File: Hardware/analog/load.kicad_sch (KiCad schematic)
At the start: 21 parts, among them J201 Würth 74651194R, J202 Würth 74651194R, Q201 IXTH80N075L2, U201 ADA4522-2, U202 LM431SC

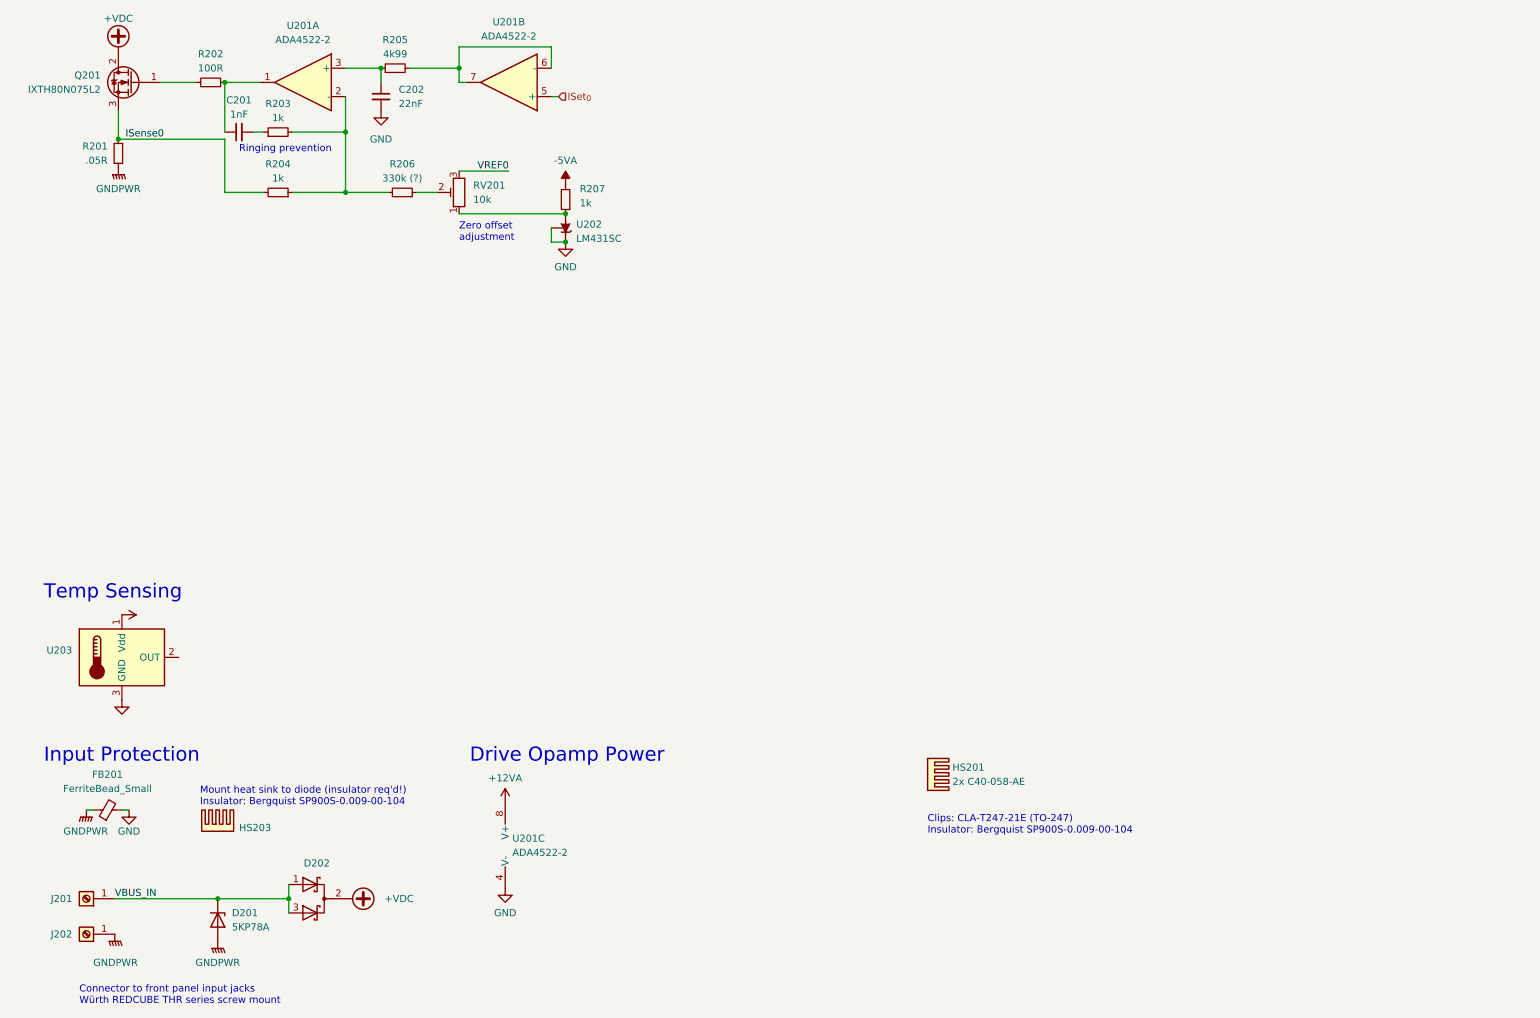
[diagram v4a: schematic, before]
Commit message: Work on layout analog board
- Moved the heatsink to be horizontal near the bottom of the analog
  board, to give more open space for the analog circuitry away from the
  hot MOSFETs

- Minor tweak to bonus display (cutout for front panel jacks)
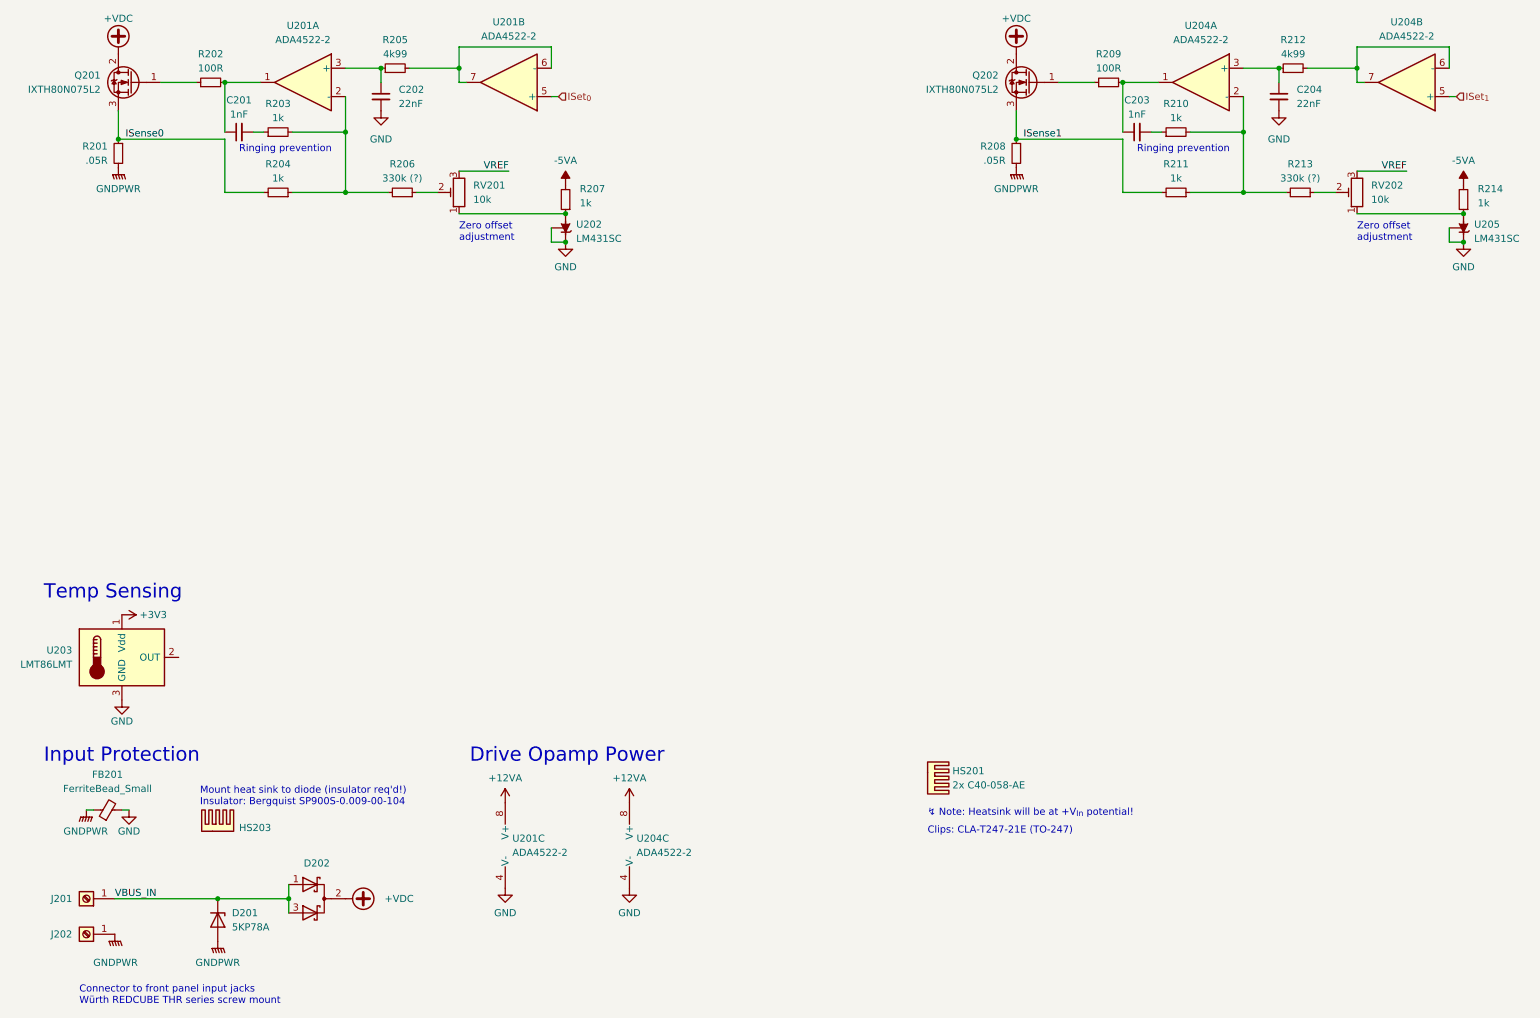
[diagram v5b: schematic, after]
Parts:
- added C203: 1nF, Capacitor_SMD:C_0805_2012Metric_Pad1.18x1.45mm_HandSolder, symbol Device:C_Small
- added C204: 22nF, Capacitor_SMD:C_0805_2012Metric_Pad1.18x1.45mm_HandSolder, symbol Device:C_Small
- added Q202: IXTH80N075L2, Package_TO_SOT_THT:TO-247-3_Vertical, symbol programmable-load:IXTH80N075L2
- added R208: .05R, programmable-load:TO-247-2_Vertical, symbol Device:R_Small
- added R209: 100R, Resistor_SMD:R_0805_2012Metric_Pad1.20x1.40mm_HandSolder, symbol Device:R_Small
- added R210, R211, R214: 1k, Resistor_SMD:R_0805_2012Metric_Pad1.20x1.40mm_HandSolder, symbol Device:R_Small
- added R212: 4k99, Resistor_SMD:R_0805_2012Metric_Pad1.20x1.40mm_HandSolder, symbol Device:R_Small
- added R213: 330k (?), Resistor_SMD:R_0805_2012Metric_Pad1.20x1.40mm_HandSolder, symbol Device:R_Small
- added RV202: 10k, programmable-load:Potentiometer_Nidec_Copal_CT94EY, symbol Device:R_Potentiometer_Trim
- added U204: ADA4522-2, Package_SO:SOIC-8_3.9x4.9mm_P1.27mm, symbol programmable-load:ADA4522-2R
- added U205: LM431SC, Package_TO_SOT_SMD:SOT-23, symbol Reference_Voltage:TL431DBZ
- U203: value (none) -> LMT86LMT
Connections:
- net +12VA: now also U204.8 (V+)
- net +VDC: now also Q202.2 (D)
- net -5VA: now also R214.2
- net GND: now also C204.2, U204.4 (V-), U205.1 (K), U205.2 (REF)
- net GNDPWR: now also R208.2
- net VREF0 renamed VREF
- net VREF: now also RV202.3
- new net: C203.1, R209.2, U204.1
- new net: R210.2, R211.1, R213.2, U204.2 (-)
- new net: C204.1, R212.1, U204.3 (+)
- new net: Q202.1 (G), R209.1
- new net: C203.2, R210.1
- new net: R213.1, RV202.2
- new net: R214.1, RV202.1, U205.3 (A)
- new net: R212.2, U204.6 (-), U204.7
- new net ISense1: Q202.3 (S), R208.1, R211.2
- new net ISet_{1}: U204.5 (+)
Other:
- note added: "Clips: CLA-T247-21E (TO-247)"
- note added: "↯ Note: Heatsink will be at +V_{In} potential!"
- note removed: "Clips: CLA-T247-21E (TO-247) Insulator: Bergquist SP900S-0.009-00-104"
- moved on the sheet: HS201

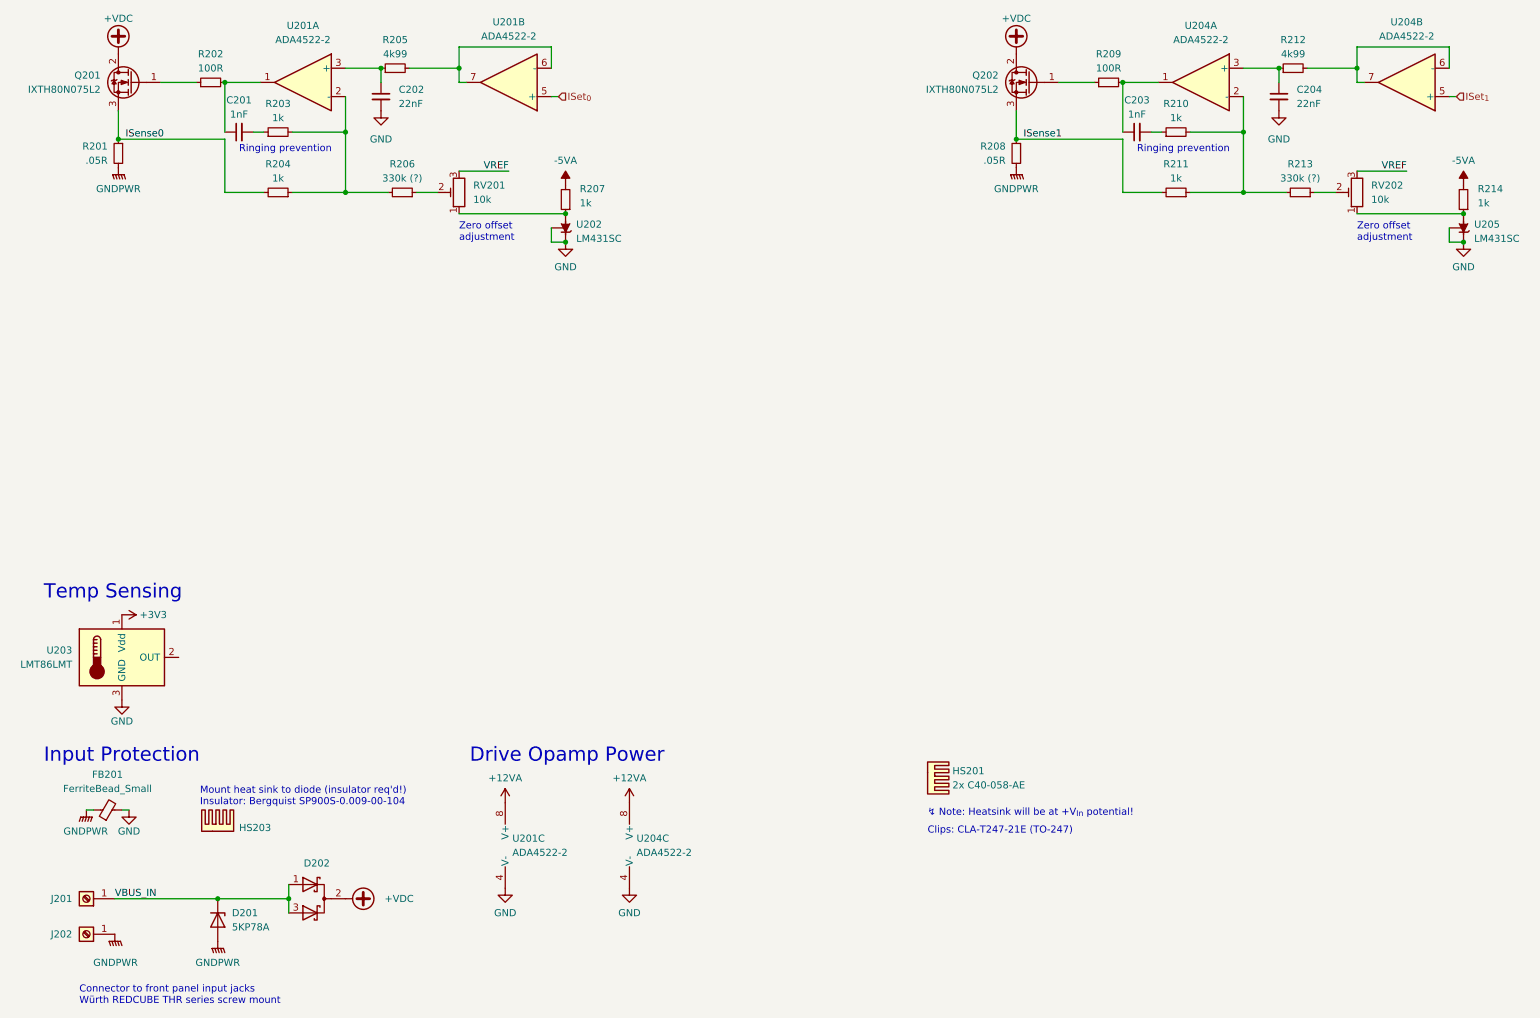
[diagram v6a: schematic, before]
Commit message: Initial pass at analog board
- Everything currently in the schematic is routed, and stuff is
  reasonably sanely laid out

- Some compromises: namely, the zero offset doesn't use the DAC
  reference for its positive, but generates a separate 2.5V via the
  shunt diodes; this is then shared between both op-amps. That avoids
  the DAC/ADC reference getting noisified

  Also, we don't have an ADC for measuring the temperature sensors yet,
  and in fact, those aren't routed out (or existent really) yet either

- TODO: add test points for drive voltages and current sense voltages
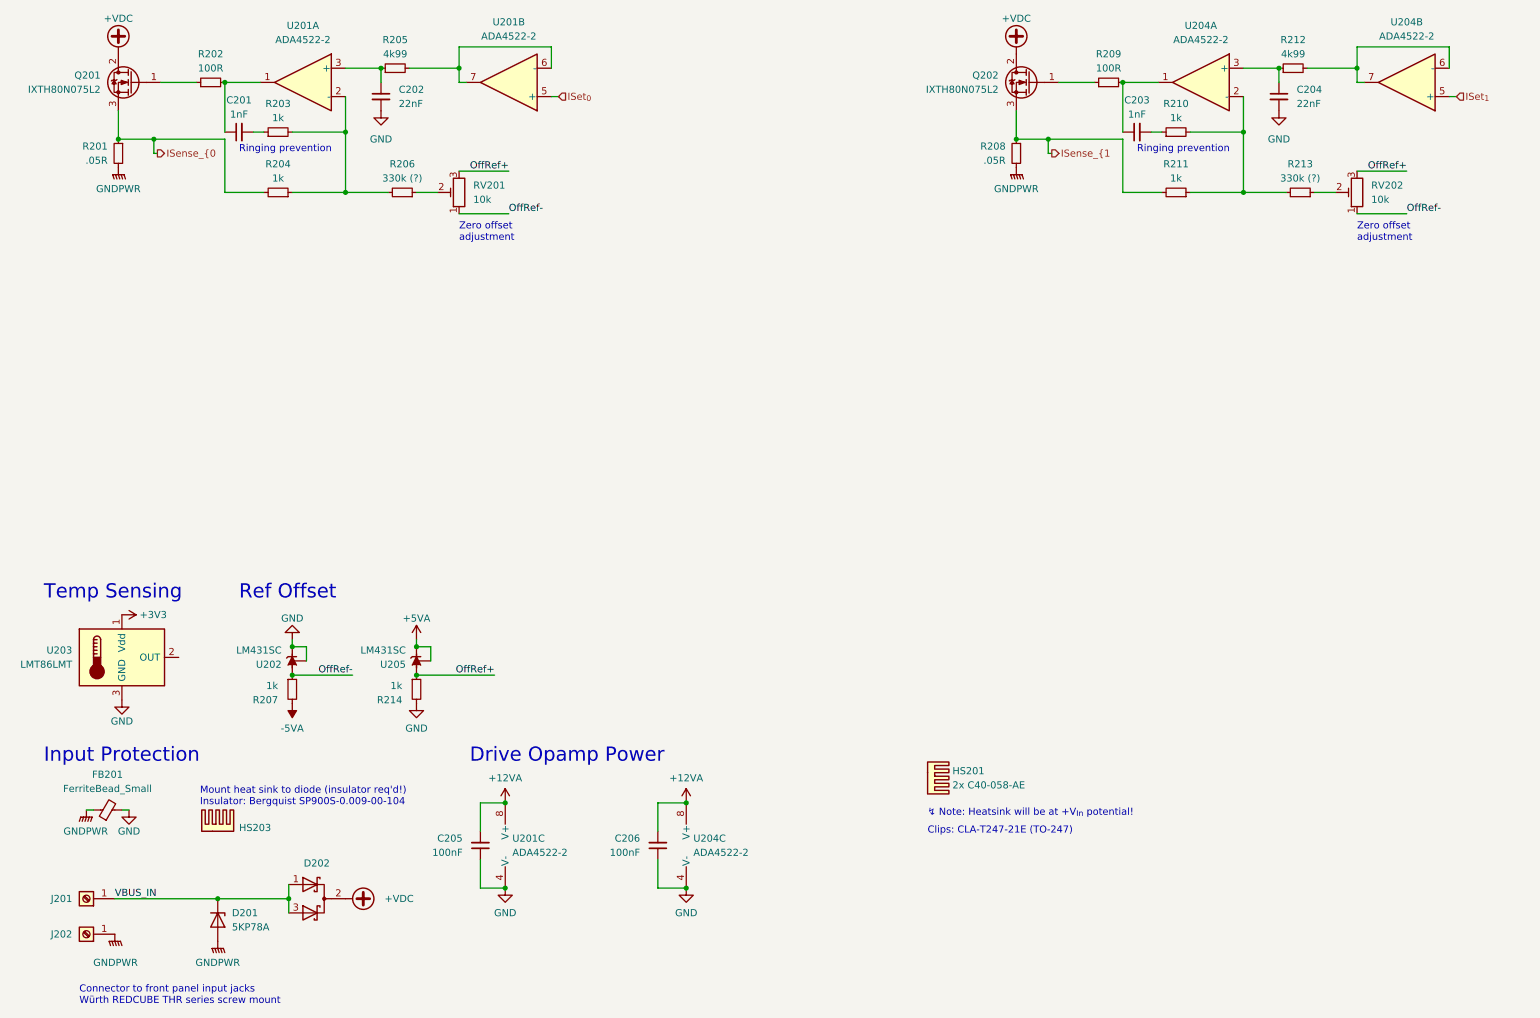
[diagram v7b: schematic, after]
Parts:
- added C205, C206: 100nF, Capacitor_SMD:C_0805_2012Metric_Pad1.18x1.45mm_HandSolder, symbol Device:C_Small
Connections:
- net VREF is gone; now on net OffRef+: RV201.3, RV202.3
- net +12VA: now also C205.2, C206.2
- net -5VA: no longer R214.2
- net GND: now also R214.2, C205.1, C206.1; no longer U205.1 (K), U205.2 (REF)
- net OffRef+: now reaches R214.1, U205.3 (A)
- net OffRef+: no longer RV202.1
- net OffRef-: now reaches R207.1, RV201.1, U202.3 (A)
- net OffRef-: now also RV202.1
- net ISense0 renamed ISense_{0
- net ISense1 renamed ISense_{1
- new net +5VA: U205.1 (K), U205.2 (REF)
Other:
- note added: "Ref Offset"
- moved on the sheet: R207, U202, U204C
